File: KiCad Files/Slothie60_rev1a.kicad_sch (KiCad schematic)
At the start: 20 parts

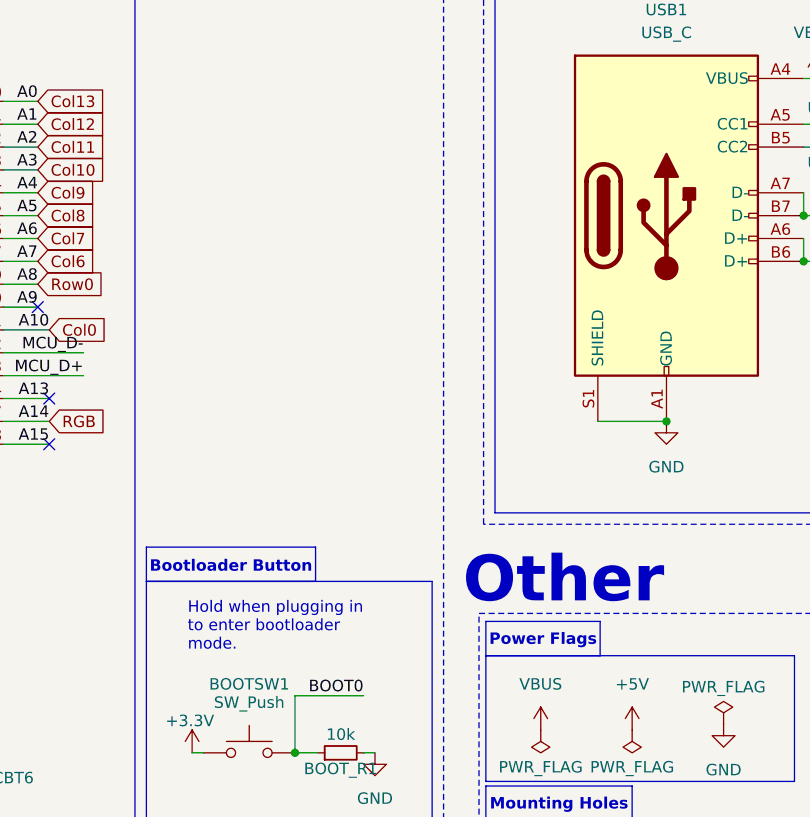
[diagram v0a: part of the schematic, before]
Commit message: Update
KiCad files had one small error, fixed it now
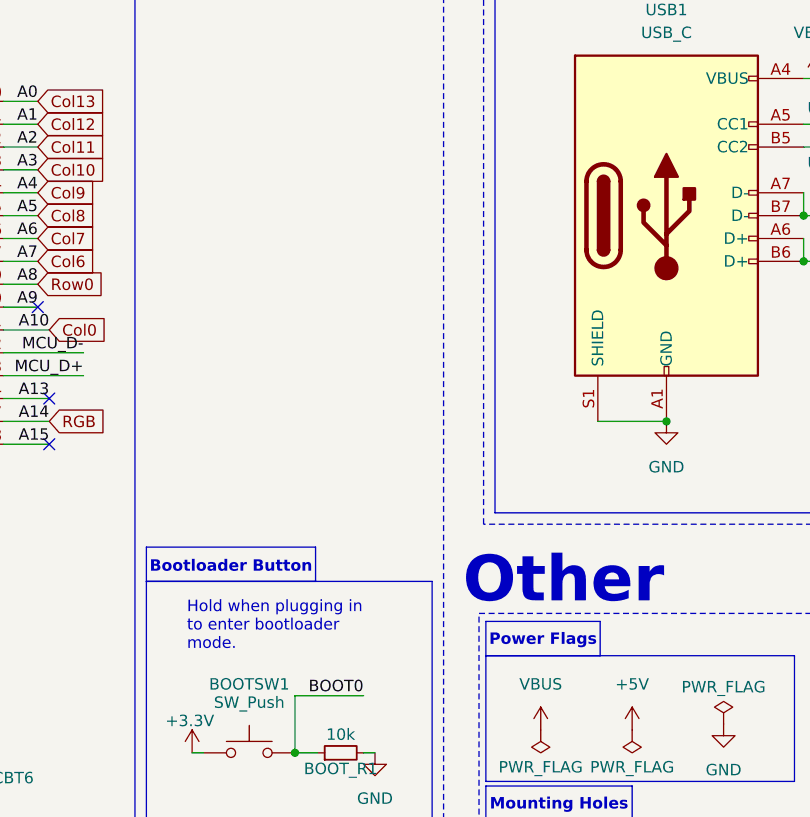
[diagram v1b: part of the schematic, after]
